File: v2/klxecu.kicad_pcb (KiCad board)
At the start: 4 copper layers, 0 parts

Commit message: V2.1 is done?
Uses the JST WPZ connector footprint instead of standard
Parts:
- added A1: Pololu_Breakout_A4988, Module:Pololu_Breakout-16_15.2x20.3mm, F.Cu at (48.3, 63.5)
- added C1: 10uF, Capacitor_Tantalum_SMD:CP_EIA-7343-31_Kemet-D, F.Cu at (57.8, 43.8)
- added C10: 100nF, Capacitor_SMD:C_0805_2012Metric_Pad1.18x1.45mm_HandSolder, B.Cu at (75.6, 78.1)
- added C11: 0.22uF, Capacitor_SMD:C_0805_2012Metric_Pad1.18x1.45mm_HandSolder, B.Cu at (109.9, 88.9)
- added C12: 0.22uF, Capacitor_SMD:C_0805_2012Metric_Pad1.18x1.45mm_HandSolder, B.Cu at (77.7, 83.2)
- added C13: 100nF, Capacitor_SMD:C_0805_2012Metric_Pad1.18x1.45mm_HandSolder, F.Cu at (109.2, 85.7)
- added C15: 100nF, Capacitor_SMD:C_0805_2012Metric_Pad1.18x1.45mm_HandSolder, F.Cu at (125.1, 84.2)
- added C16: 0.33uF, Capacitor_SMD:C_0805_2012Metric_Pad1.18x1.45mm_HandSolder, F.Cu at (110.5, 88.9)
- added C18: 0.22uF, Capacitor_SMD:C_0805_2012Metric_Pad1.18x1.45mm_HandSolder, F.Cu at (125.1, 88.3)
- added C19: 0.1uf, Capacitor_SMD:C_0805_2012Metric, F.Cu at (90.2, 65.4)
- added C2: 0.1uF, Capacitor_SMD:C_0805_2012Metric, F.Cu at (64.1, 45.1)
- added C20: 1uF, Capacitor_SMD:C_0805_2012Metric_Pad1.18x1.45mm_HandSolder, B.Cu at (46.3, 102.9)
- added C21: 100uF, Capacitor_THT:CP_Radial_D5.0mm_P2.50mm, F.Cu at (66.0, 68.6)
- added C3: 0.1uF, Capacitor_SMD:C_0805_2012Metric, F.Cu at (78.7, 48.3)
- added C4: 47uF, Capacitor_Tantalum_SMD:CP_EIA-3528-21_Kemet-B, F.Cu at (74.9, 48.9)
- added C5: 100nF, Capacitor_SMD:C_0805_2012Metric_Pad1.18x1.45mm_HandSolder, F.Cu at (116.8, 84.2)
- added C6: 100nF, Capacitor_SMD:C_0805_2012Metric_Pad1.18x1.45mm_HandSolder, F.Cu at (101.4, 87.6)
- added C7: 100nF, Capacitor_SMD:C_0805_2012Metric_Pad1.18x1.45mm_HandSolder, B.Cu at (102.2, 88.9)
- added C8: 0.22uF, Capacitor_SMD:C_0805_2012Metric_Pad1.18x1.45mm_HandSolder, F.Cu at (116.8, 88.3)
- added C9: 0.22uF, Capacitor_SMD:C_0805_2012Metric_Pad1.18x1.45mm_HandSolder, F.Cu at (104.8, 88.9)
- added D1: B130-13-F, Diode_SMD:D_SMA, F.Cu at (73.0, 43.8)
- added D2: 1SMB5919BT3G, Diode_SMD:D_SMB, F.Cu at (100.3, 48.9)
- added D3: 1N5818, Diode_THT:D_DO-41_SOD81_P7.62mm_Horizontal, F.Cu at (89.5, 88.3)
- added D4: 1N5818, Diode_THT:D_DO-41_SOD81_P7.62mm_Horizontal, F.Cu at (81.9, 84.5)
- added IC1: SP721, Package_DIP:DIP-8_W7.62mm, F.Cu at (114.9, 99.7)
- added J1: CAM_SENSOR_IN, Connector_PinHeader_2.54mm:PinHeader_1x02_P2.54mm_Vertical, F.Cu at (59.1, 89.1)
- added J2: Conn_01x06, Connector_PinHeader_2.54mm:PinHeader_1x06_P2.54mm_Vertical, F.Cu at (120.7, 56.5)
- added J3: DIP8, Package_DIP:DIP-8_W7.62mm_Socket, F.Cu at (94.6, 107.3)
- added J4: Conn_02x04_Counter_Clockwise, mega_2560:vr_conditioner, F.Cu at (48.2, 83.4)
- added J5: TACH_OUT, Connector_PinHeader_2.54mm:PinHeader_1x01_P2.54mm_Vertical, F.Cu at (67.9, 90.2)
- added JP1: Jumper_3_Open, Connector_PinHeader_2.54mm:PinHeader_1x03_P2.54mm_Vertical, F.Cu at (70.5, 66.0)
- added PAD1: MountingHole_4.3mm_M4_Pad, MountingHole:MountingHole_4.3mm_M4_Pad, F.Cu at (121.9, 45.7)
- added PAD2: MountingHole_4.3mm_M4_Pad, MountingHole:MountingHole_4.3mm_M4_Pad, F.Cu at (121.9, 109.2)
- added PAD3: MountingHole_2.2mm_M2_Pad, MountingHole:MountingHole_2.2mm_M2_Pad, F.Cu at (29.8, 111.1)
- added PAD4: MountingHole_2.2mm_M2_Pad, MountingHole:MountingHole_2.2mm_M2_Pad, F.Cu at (29.8, 43.8)
- added Q1: SSM3K357R, Package_TO_SOT_SMD:SOT-23, F.Cu at (66.0, 104.1)
- added Q2: SSM3K357R, Package_TO_SOT_SMD:SOT-23, F.Cu at (71.1, 99.7)
- added Q3: STP62NS04Z, Package_TO_SOT_THT:TO-220-3_Vertical, F.Cu at (56.5, 105.4)
- added Q4: SSM3K357R, Package_TO_SOT_SMD:SOT-23, F.Cu at (66.0, 99.7)
- added Q5: SSM3K357R, Package_TO_SOT_SMD:SOT-23, F.Cu at (71.1, 104.1)
- added Q6: SSM3K357R, Package_TO_SOT_SMD:SOT-23, F.Cu at (67.9, 94.0)
- added R1: 2k, Resistor_SMD:R_0805_2012Metric, F.Cu at (123.8, 56.5)
- added R10: 470, Resistor_SMD:R_0805_2012Metric_Pad1.20x1.40mm_HandSolder, B.Cu at (75.6, 80.6)
- added R11: 2.49K, Resistor_SMD:R_0805_2012Metric_Pad1.20x1.40mm_HandSolder, F.Cu at (122.6, 84.2)
- added R12: 470, Resistor_SMD:R_0805_2012Metric_Pad1.20x1.40mm_HandSolder, F.Cu at (108.0, 88.9)
- added R14: 470, Resistor_SMD:R_0805_2012Metric_Pad1.20x1.40mm_HandSolder, F.Cu at (122.6, 88.3)
- added R15: 1k, Resistor_SMD:R_0805_2012Metric_Pad1.20x1.40mm_HandSolder, F.Cu at (86.1, 65.4)
- added R16: 100K, Resistor_SMD:R_0805_2012Metric, F.Cu at (59.4, 101.0)
- added R17: 1K, Resistor_SMD:R_0805_2012Metric, F.Cu at (59.4, 104.8)
- added R18: 1K, Resistor_SMD:R_0805_2012Metric_Pad1.20x1.40mm_HandSolder, F.Cu at (48.9, 109.2)
- added R19: 100K, Resistor_SMD:R_0805_2012Metric_Pad1.20x1.40mm_HandSolder, F.Cu at (45.1, 109.2)
- added R2: 1k, Resistor_SMD:R_0805_2012Metric, F.Cu at (104.8, 56.5)
- added R20: 10R, Resistor_SMD:R_0805_2012Metric, F.Cu at (38.1, 103.5)
- added R21: 10K, Resistor_SMD:R_0805_2012Metric, F.Cu at (67.3, 87.0)
- added R3: 2.49K, Resistor_SMD:R_0805_2012Metric_Pad1.20x1.40mm_HandSolder, F.Cu at (114.3, 84.2)
- added R4: 3.9K, Resistor_SMD:R_0805_2012Metric_Pad1.20x1.40mm_HandSolder, B.Cu at (107.3, 84.5)
- added R5: 1K, Resistor_SMD:R_0805_2012Metric_Pad1.20x1.40mm_HandSolder, B.Cu at (104.8, 88.9)
- added R6: 470, Resistor_SMD:R_0805_2012Metric_Pad1.20x1.40mm_HandSolder, F.Cu at (114.3, 88.3)
- added R7: 470, Resistor_SMD:R_0805_2012Metric_Pad1.20x1.40mm_HandSolder, F.Cu at (101.2, 90.2)
- added R8: 470, Resistor_SMD:R_0805_2012Metric_Pad1.20x1.40mm_HandSolder, B.Cu at (107.3, 88.9)
- added R9: 2.49K, Resistor_SMD:R_0805_2012Metric_Pad1.20x1.40mm_HandSolder, B.Cu at (78.7, 79.4)
- added RV1: Varistor, Varistor:RV_Disc_D15.5mm_W4.7mm_P7.5mm, F.Cu at (40.7, 42.8)
- added U1: S36B-WPZK-A, mega_2560:S36B-WPZK-A, F.Cu at (33.0, 76.2)
- added U2: LM2940S-5.0/NOPB, Package_TO_SOT_SMD:TO-263-3_TabPin2, F.Cu at (88.7, 47.0)
- added U3: Arduino Mega 2560 Pro, mega_2560:mega_2560_pro, F.Cu at (99.7, 78.1)
- added U4: TC4424AVPA, Package_DIP:DIP-8_W7.62mm_Socket, F.Cu at (41.3, 106.7)
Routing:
- net GND: track 0.00 -> 195.2 mm, vias 0 -> 21
- net +12V: track 0.00 -> 173.9 mm, vias 0 -> 2
- net NEUTRAL: track 0.00 -> 122.3 mm
- net CLT: track 0.00 -> 121.3 mm
- net IAT: track 0.00 -> 116.1 mm
- net VDOWN: track 0.00 -> 116.0 mm
- net VSS: track 0.00 -> 97.5 mm, vias 0 -> 1
- net SIDE-SW: track 0.00 -> 96.9 mm
- net MAP: track 0.00 -> 84.8 mm, vias 0 -> 2
- net KILL-SW: track 0.00 -> 83.4 mm
- net TPS: track 0.00 -> 78.2 mm, vias 0 -> 2
- net +5V: track 0.00 -> 78.0 mm, vias 0 -> 3
- net INJ-ARD-D8: track 0.00 -> 77.8 mm, vias 0 -> 1
- net MIL: track 0.00 -> 74.7 mm, vias 0 -> 1
- net SELF-DIAG: track 0.00 -> 74.4 mm, vias 0 -> 1
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- added copper zone on In2.Cu, net +5V
- added copper zone on B.Cu, net GND
- added copper zone on F.Cu, net GND
- added copper zone on In1.Cu, net GND
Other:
- board outline added: 101.6 x 74.9 mm
- board text added: "klxecu v2"

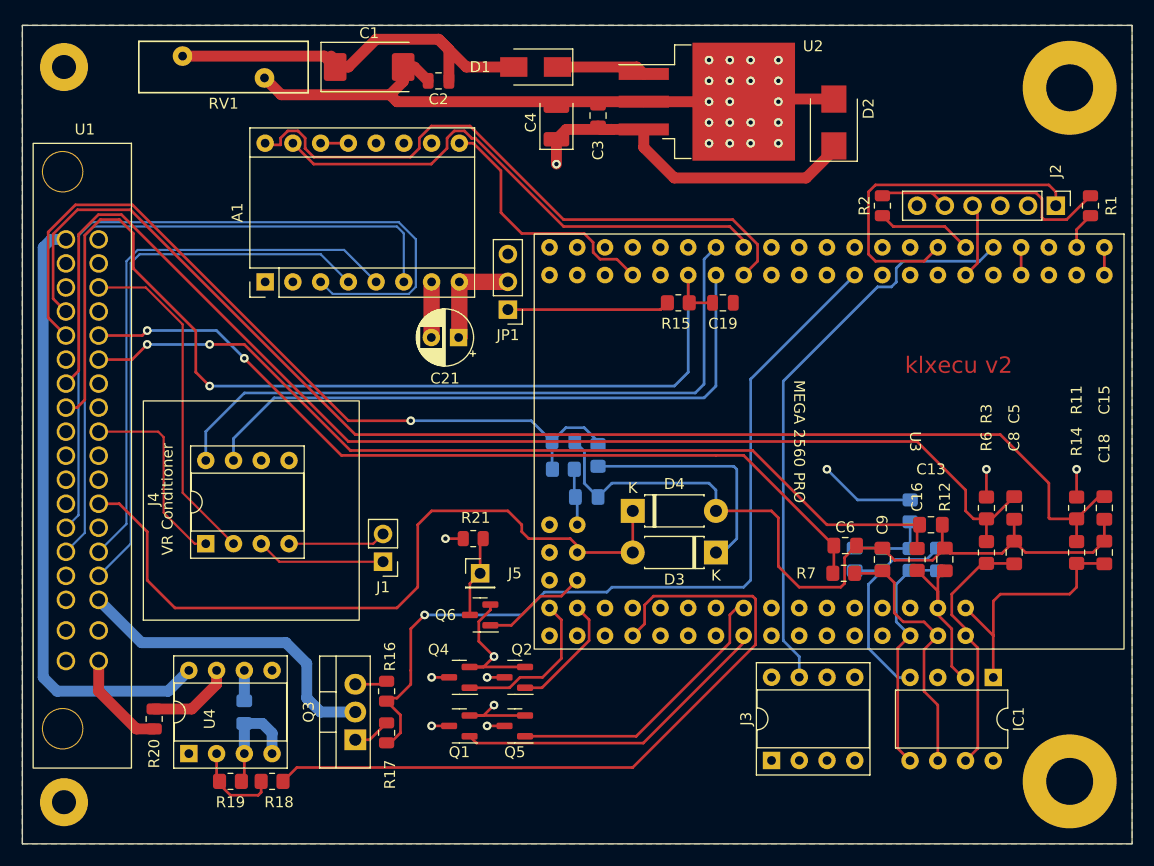
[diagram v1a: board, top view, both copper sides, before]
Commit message: Re-add traces for oxygen sensor
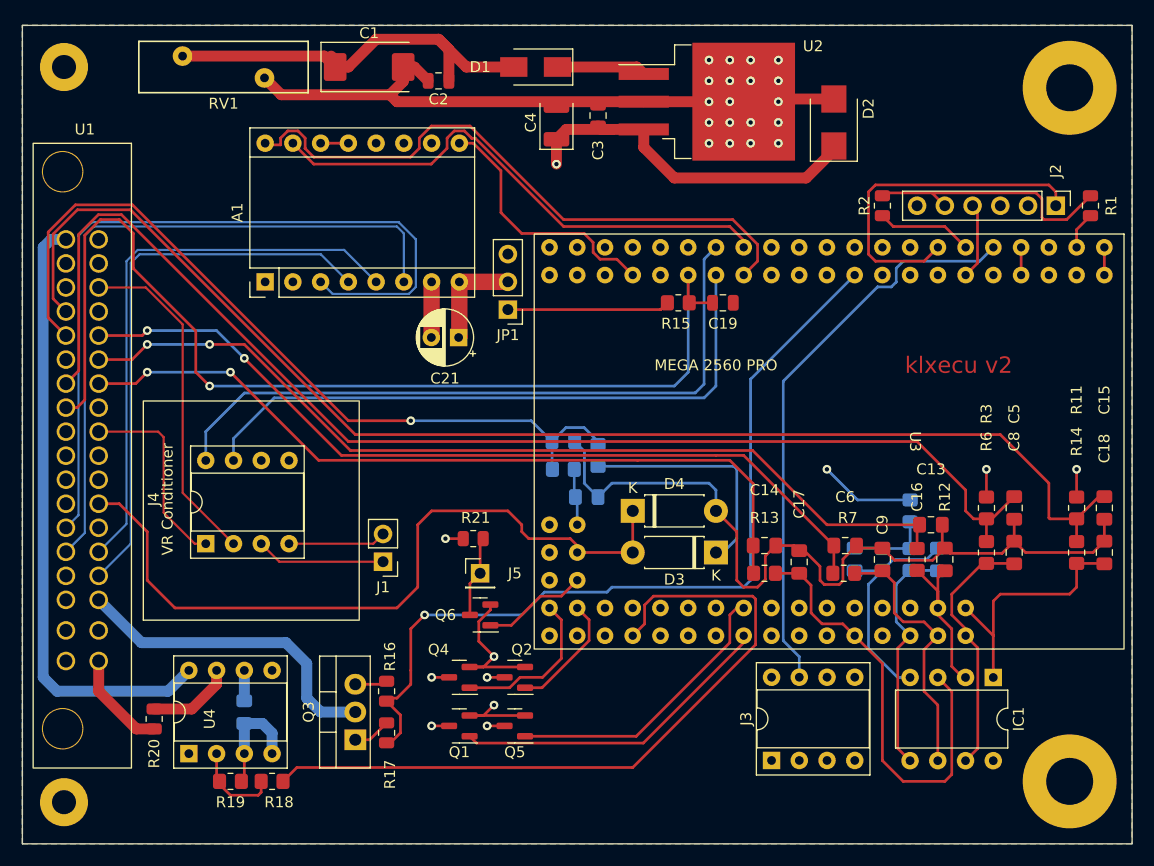
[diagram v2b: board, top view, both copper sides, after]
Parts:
- added C14: 100nF, Capacitor_SMD:C_0805_2012Metric_Pad1.18x1.45mm_HandSolder, F.Cu at (94.0, 87.6)
- added C17: 0.33uF, Capacitor_SMD:C_0805_2012Metric_Pad1.18x1.45mm_HandSolder, F.Cu at (97.2, 89.1)
- added R13: 470, Resistor_SMD:R_0805_2012Metric_Pad1.20x1.40mm_HandSolder, F.Cu at (94.0, 90.2)
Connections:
- IC1 pad 3: unconnected-(IC1-Pad3) -> O2S-ARD-A8
- U1 pad 7: unconnected-(U1-Pad7) -> O2S
- U3 pad A8: unconnected-(U3-PadA8) -> O2S-ARD-A8
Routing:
- net O2S: track 0.00 -> 72.8 mm, vias 0 -> 2
- net O2S-ARD-A8: track 0.00 -> 40.4 mm
- net GND: track 195.2 -> 200.0 mm

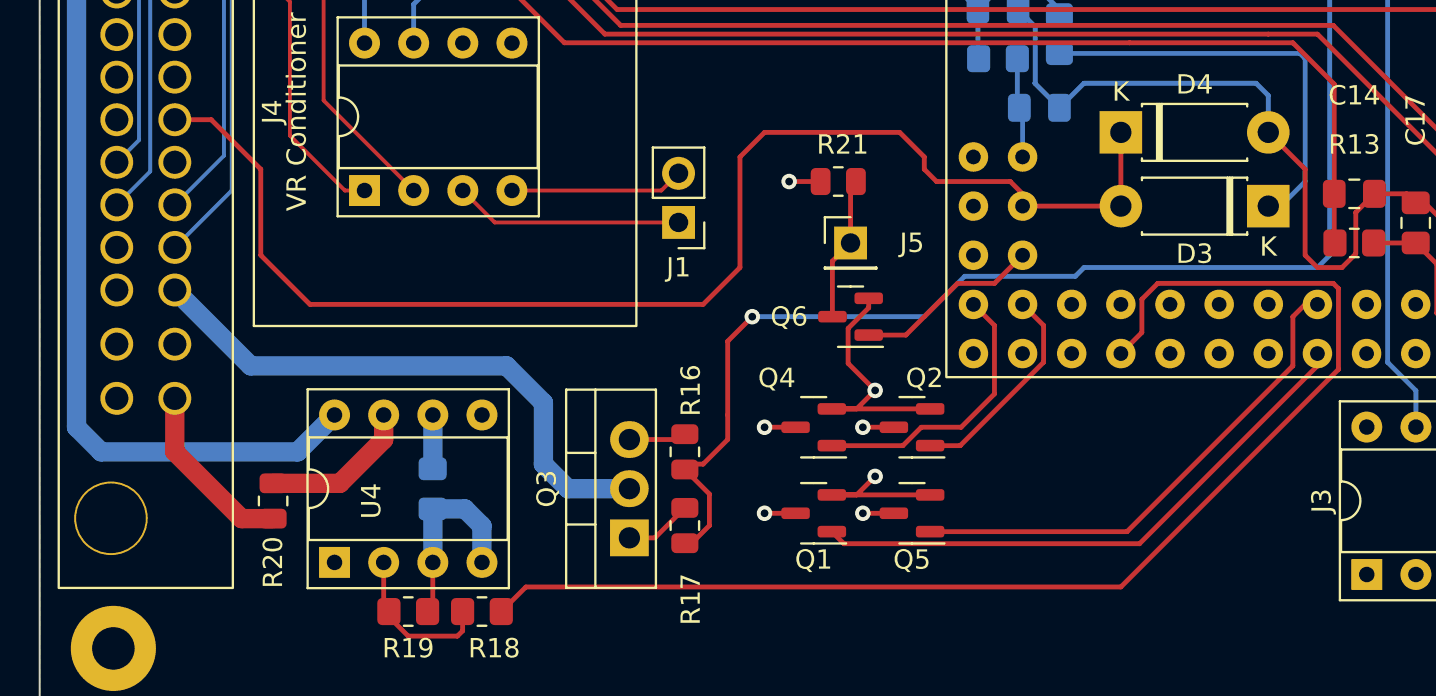
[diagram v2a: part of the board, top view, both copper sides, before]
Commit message: Add control of air switching valve
Plus a jumper to lock the valve closed
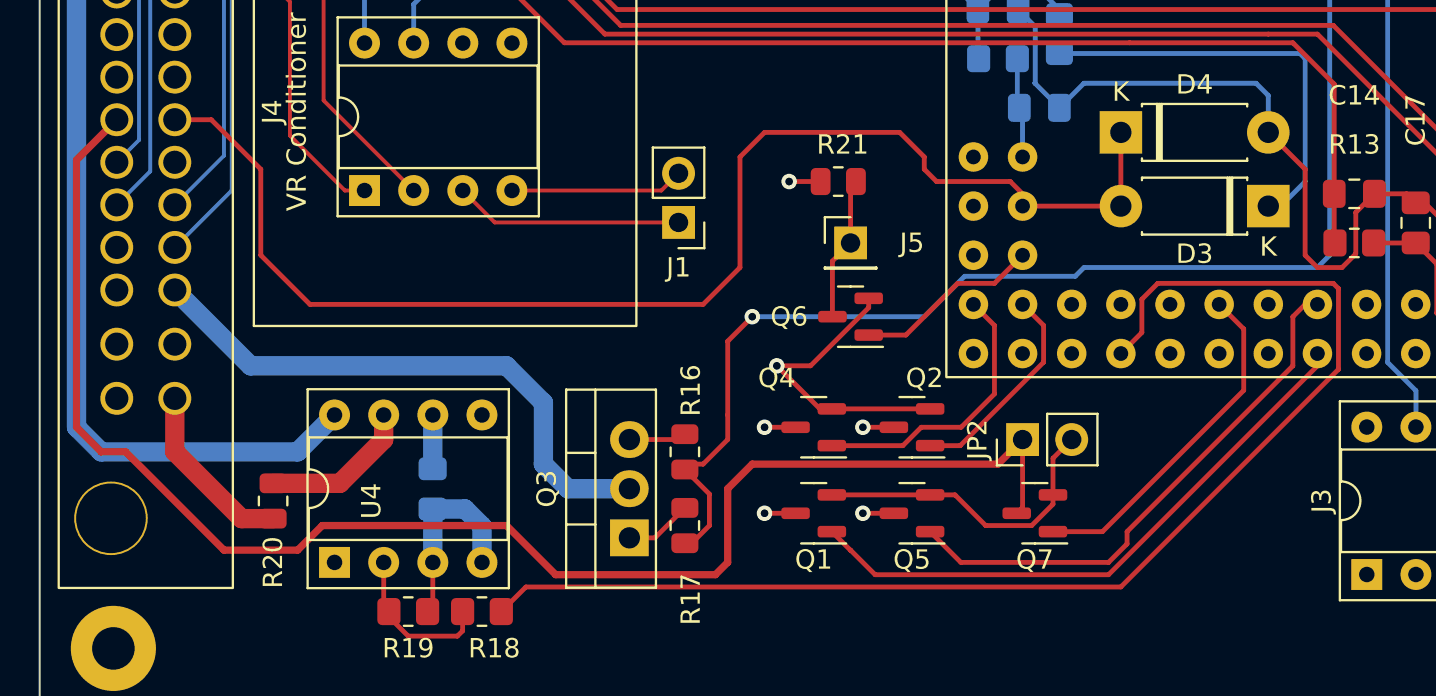
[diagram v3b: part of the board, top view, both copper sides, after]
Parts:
- added JP2: Jumper_2_Open, Connector_PinHeader_2.54mm:PinHeader_1x02_P2.54mm_Vertical, F.Cu at (76.8, 100.3)
- added Q7: SSM3K357R, Package_TO_SOT_SMD:SOT-23, F.Cu at (77.5, 104.1)
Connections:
- U1 pad 30: unconnected-(U1-Pad30) -> AIRSW
- U3 pad D37: unconnected-(U3-PadD37) -> AIRSW-ARD-D37
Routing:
- net AIRSW: track 0.00 -> 78.9 mm
- net AIRSW-ARD-D37: track 0.00 -> 17.9 mm
- net GND: track 200.0 -> 210.4 mm, vias 21 -> 20
- net TWARN-ARD-D33: track 26.4 -> 28.1 mm
- net MIL-ARD-D32: track 29.8 -> 31.1 mm

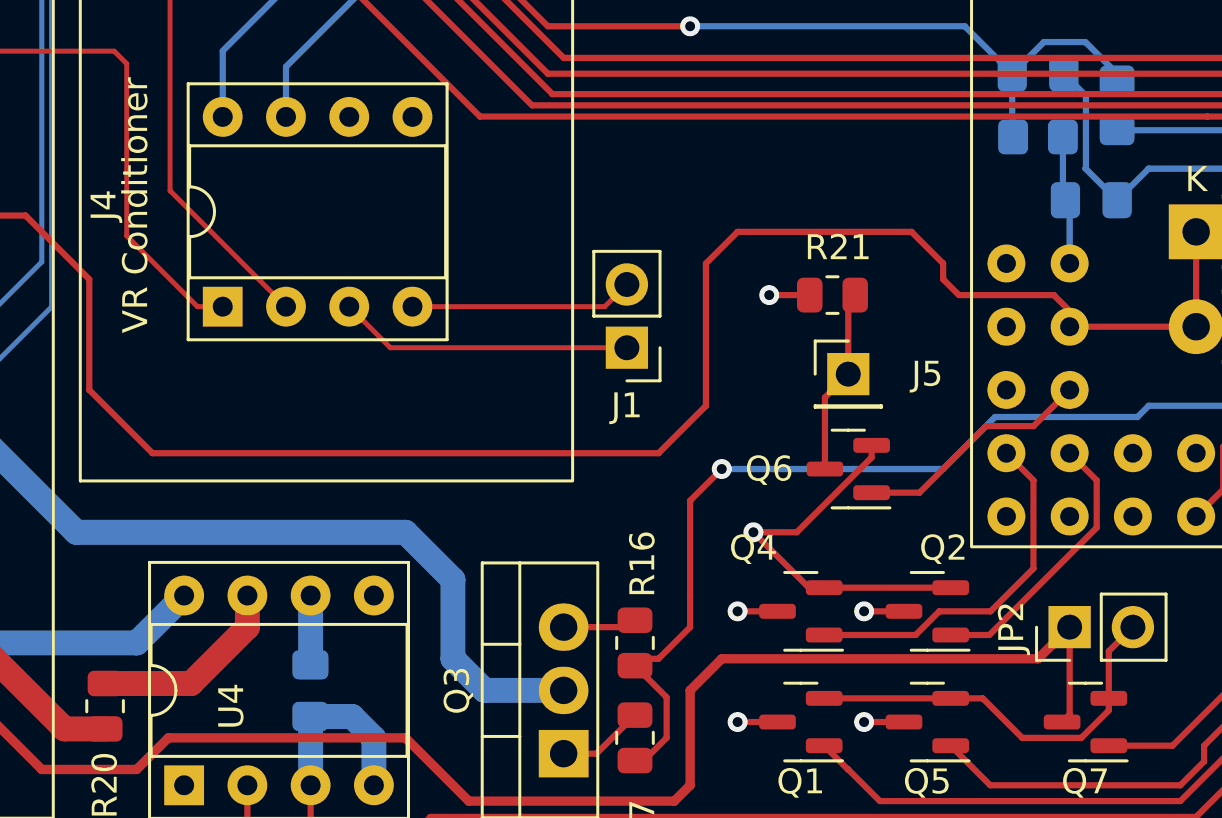
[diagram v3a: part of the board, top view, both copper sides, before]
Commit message: add 12v/5v/GND options to cam sensor connector
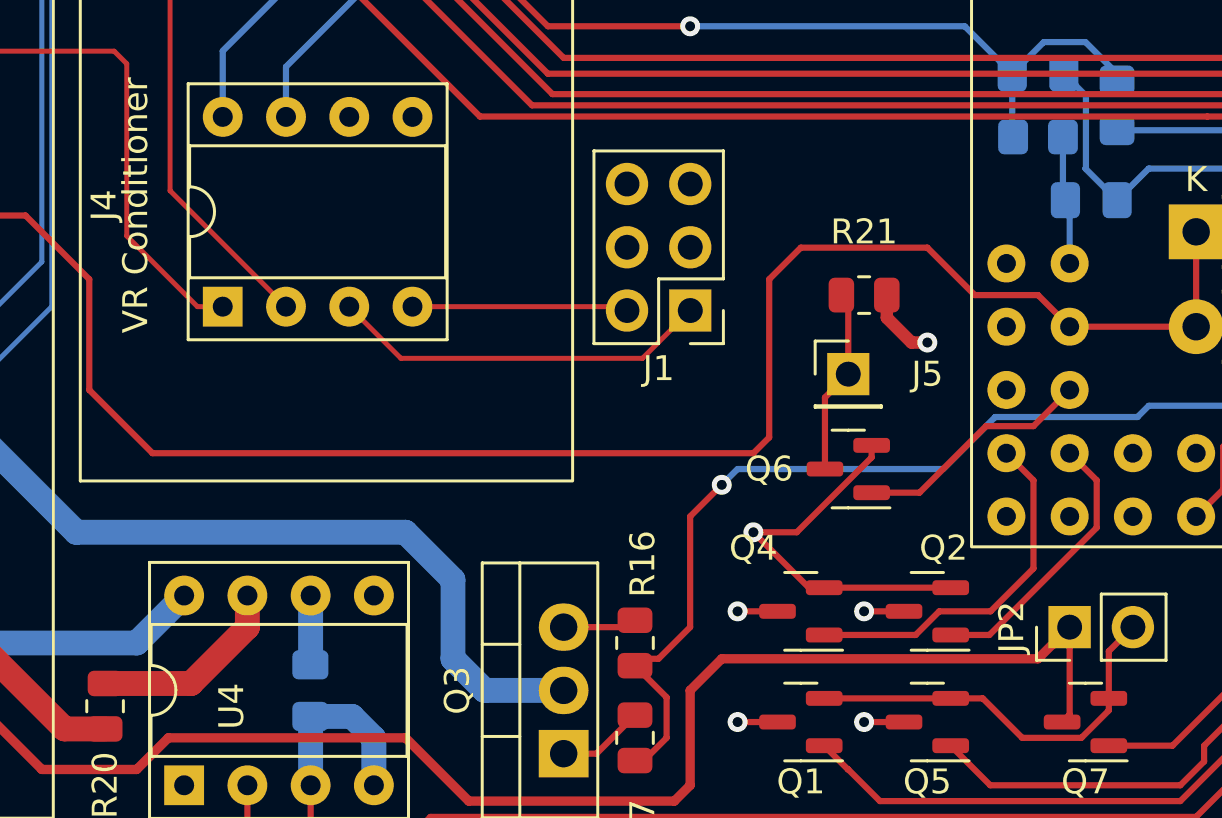
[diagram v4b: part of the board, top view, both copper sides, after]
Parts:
- J1: value CAM_SENSOR_IN -> cam_sensor; footprint Connector_PinHeader_2.54mm:PinHeader_1x02_P2.54mm_Vertical -> Connector_PinHeader_2.54mm:PinHeader_2x03_P2.54mm_Vertical
- moved J1 2.95 mm to (61.6, 87.6)
- moved R21 1.27 mm to (68.6, 87.0), turned to 0 degrees
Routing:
- net +12V: track 173.9 -> 192.0 mm
- net CAM+: track 11.8 -> 15.3 mm
- net CLUTCH-SW: track 68.6 -> 67.7 mm
